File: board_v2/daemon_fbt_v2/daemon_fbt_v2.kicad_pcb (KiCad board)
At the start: 2 copper layers, 58 parts, among them IC1 NPM1100-QDAA-R7, IC2 nRF52840-QFAA-F-R7, IC3 MX25R6435FZAIL0-TR, J1 P70-5100045, J2 P70-5100045, J3 150mAh, Q1 FDV303N, U1 BMM350, U2 BHI360, Y1 ECS-320-8-37B2-CTN-TR

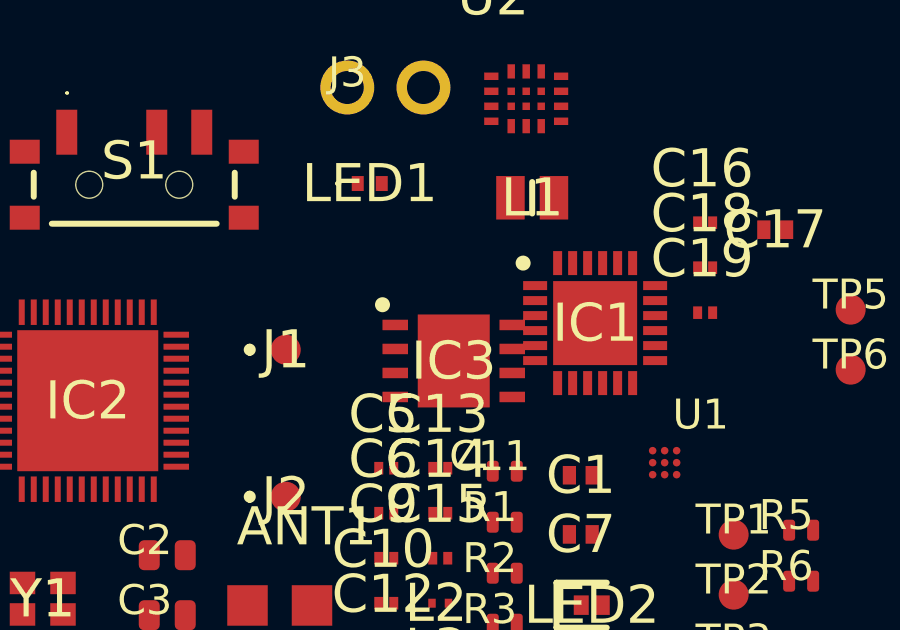
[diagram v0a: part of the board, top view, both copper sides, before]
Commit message: update flash memory from 64Mbit to 2Mbit and create footprint
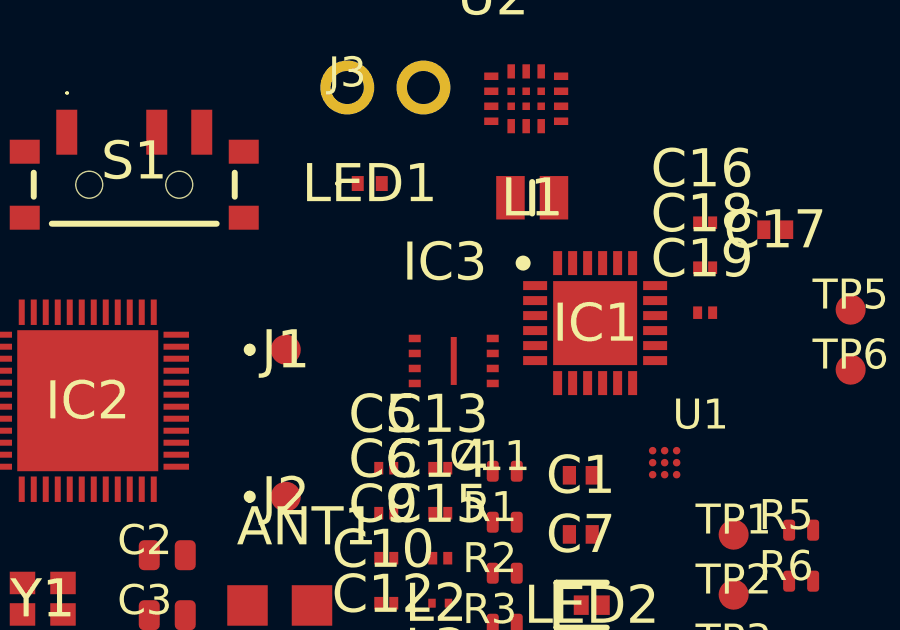
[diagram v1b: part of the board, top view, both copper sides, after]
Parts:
- IC3: value MX25R6435FZAIL0-TR -> MX25U2035FZUI-TR; footprint the_backrooms:SON80P400X400X60-9N -> the_backrooms:SON50P200X300X60-9N
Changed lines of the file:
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@@
     )
   )
-  (footprint "the_backrooms:SON80P400X400X60-9N" (layer "F.Cu")
+  (footprint "the_backrooms:SON50P200X300X60-9N" (layer "F.Cu")
     (at 39.57 33.01)
-    (descr "8-LAND USON (4x4mm)")
+    (descr "8-LAND USON (2x3mm)")
     (tags "Integrated Circuit")
     (property "Arrow Part Number" "")
     (property "Arrow Price/Stock" "")
+    (property "Description" "")
     (property "Height" "0.6")
     (property "Manufacturer_Name" "Macronix")
-    (property "Manufacturer_Part_Number" "MX25R6435FZAIL0-TR")
-    (property "Mfr. No." "MX25R6435FZAIL0-TR")
-    (property "Mouser Part Number" "95-25R6435FZAIL0TR")
-    (property "Mouser Price/Stock" "https://www.mouser.co.uk/ProductDetail/Macronix/MX25R6435FZAIL0-TR?qs=mELouGlnn3cK%252BXKdc9RzBg%3D%3D")
+    (property "Manufacturer_Part_Number" "MX25U2035FZUI-TR")
+    (property "Mfr. No." "MX25U2035FZUI-TR")
+    (property "Mouser Part Number" "MX25U2035FZUI-TR")
+    (property "Mouser Price/Stock" "")
+    (property "Package/Case" "")
     (property "Sheetfile" "daemon_fbt_v2.kicad_sch")
     (property "Sheetname" "")
     (property "ki_description" "NOR Flash Serial NOR 1.65V-3.6V 64Mbit x4 I/O USON-8 4x4mm")
     (attr smd)
-    (fp_text reference "IC3" (at 0 0) (layer "F.SilkS")
+    (fp_text reference "IC3" (at -0.3 -3.3) (layer "F.SilkS")
         (effects (font (size 1.27 1.27) (thickness 0.254)))
     )
-    (fp_text value "MX25R6435FZAIL0-TR" (at 0 0) (layer "F.SilkS") hide
+    (fp_text value "MX25U2035FZUI-TR" (at 0.2 3.3) (layer "F.SilkS") hide
         (effects (font (size 1.27 1.27) (thickness 0.254)))
     )
-    (fp_text user "${REFERENCE}" (at 0 0) (layer "F.Fab")
+    (fp_text user "${REFERENCE}" (at -0.1 3.4) (layer "F.Fab")
         (effects (font (size 1.27 1.27) (thickness 0.254)))
     )
-    (fp_circle (center -2.375 -1.875) (end -2.375 -1.75)
-      (stroke (width 0.25) (type solid)) (fill none) (layer "F.SilkS"))
-    (fp_line (start -2.625 -2.3) (end 2.625 -2.3)
-      (stroke (width 0.05) (type solid)) (layer "F.CrtYd"))
-    (fp_line (start -2.625 2.3) (end -2.625 -2.3)
-      (stroke (width 0.05) (type solid)) (layer "F.CrtYd"))
-    (fp_line (start 2.625 -2.3) (end 2.625 2.3)
-      (stroke (width 0.05) (type solid)) (layer "F.CrtYd"))
-    (fp_line (start 2.625 2.3) (end -2.625 2.3)
-      (stroke (width 0.05) (type solid)) (layer "F.CrtYd"))
-    (fp_line (start -2 -2) (end 2 -2)
-      (stroke (width 0.1) (type solid)) (layer "F.Fab"))
-    (fp_line (start -2 -1) (end -1 -2)
-      (stroke (width 0.1) (type solid)) (layer "F.Fab"))
-    (fp_line (start -2 2) (end -2 -2)
-      (stroke (width 0.1) (type solid)) (layer "F.Fab"))
-    (fp_line (start 2 -2) (end 2 2)
-      (stroke (width 0.1) (type solid)) (layer "F.Fab"))
-    (fp_line (start 2 2) (end -2 2)
-      (stroke (width 0.1) (type solid)) (layer "F.Fab"))
-    (pad "1" smd rect (at -1.95 -1.2 90) (size 0.35 0.85) (layers "F.Cu" "F.Paste" "F.Mask")
+    (fp_rect (start -1.5 -1) (end 1.5 1)
+      (stroke (width 0.1) (type default)) (fill none) (layer "Margin"))
+    (pad "1" smd rect (at -1.3 -0.75 90) (size 0.25 0.4) (layers "F.Cu" "F.Paste" "F.Mask")
       (net 48 "/QSPI_~{CS}") (pinfunction "CS#") (pintype "passive"))
-    (pad "2" smd rect (at -1.95 -0.4 90) (size 0.35 0.85) (layers "F.Cu" "F.Paste" "F.Mask")
+    (pad "2" smd rect (at -1.3 -0.25 90) (size 0.25 0.4) (layers "F.Cu" "F.Paste" "F.Mask")
       (net 51 "/QSPI_1") (pinfunction "SO/SIO1") (pintype "passive"))
-    (pad "3" smd rect (at -1.95 0.4 90) (size 0.35 0.85) (layers "F.Cu" "F.Paste" "F.Mask")
+    (pad "3" smd rect (at -1.3 0.25 90) (size 0.25 0.4) (layers "F.Cu" "F.Paste" "F.Mask")
       (net 52 "/QSPI_2") (pinfunction "WP#/SIO2") (pintype "passive"))
-    (pad "4" smd rect (at -1.95 1.2 90) (size 0.35 0.85) (layers "F.Cu" "F.Paste" "F.Mask")
+    (pad "4" smd rect (at -1.3 0.75 90) (size 0.25 0.4) (layers "F.Cu" "F.Paste" "F.Mask")
       (net 5 "GND") (pinfunction "GND") (pintype "passive"))
-    (pad "5" smd rect (at 1.95 1.2 90) (size 0.35 0.85) (layers "F.Cu" "F.Paste" "F.Mask")
+    (pad "5" smd rect (at 1.3 0.75 90) (size 0.25 0.4) (layers "F.Cu" "F.Paste" "F.Mask")
       (net 50 "/QSPI_0") (pinfunction "SI/SIO0") (pintype "passive"))
-    (pad "6" smd rect (at 1.95 0.4 90) (size 0.35 0.85) (layers "F.Cu" "F.Paste" "F.Mask")
+    (pad "6" smd rect (at 1.3 0.25 90) (size 0.25 0.4) (layers "F.Cu" "F.Paste" "F.Mask")
       (net 49 "/QSPI_CLK") (pinfunction "SCLK") (pintype "passive"))
-    (pad "7" smd rect (at 1.95 -0.4 90) (size 0.35 0.85) (layers "F.Cu" "F.Paste" "F.Mask")
+    (pad "7" smd rect (at 1.3 -0.25 90) (size 0.25 0.4) (layers "F.Cu" "F.Paste" "F.Mask")
       (net 53 "/QSPI_3") (pinfunction "RESET#/SIO3__OR_HOLD#/SIO3") (pintype "passive"))
-    (pad "8" smd rect (at 1.95 -1.2 90) (size 0.35 0.85) (layers "F.Cu" "F.Paste" "F.Mask")
+    (pad "8" smd rect (at 1.3 -0.75 90) (size 0.25 0.4) (layers "F.Cu" "F.Paste" "F.Mask")
       (net 7 "+1V8") (pinfunction "VCC") (pintype "passive"))
-    (pad "9" smd rect (at 0 0) (size 2.4 3.1) (layers "F.Cu" "F.Paste" "F.Mask")
+    (pad "9" smd rect (at 0 0) (size 0.2 1.6) (layers "F.Cu" "F.Paste" "F.Mask")
       (net 5 "GND") (pinfunction "EP") (pintype "passive"))
-    (model "/home/denji/Documents/kicad_lib/3d/MX25R6435FZAIL0-TR.stp"
-      (offset (xyz 0 0 0))
-      (scale (xyz 1 1 1))
-      (rotate (xyz 0 0 0))
-    )
   )
   (footprint "the_backrooms:FHR1105PTR" (layer "F.Cu")

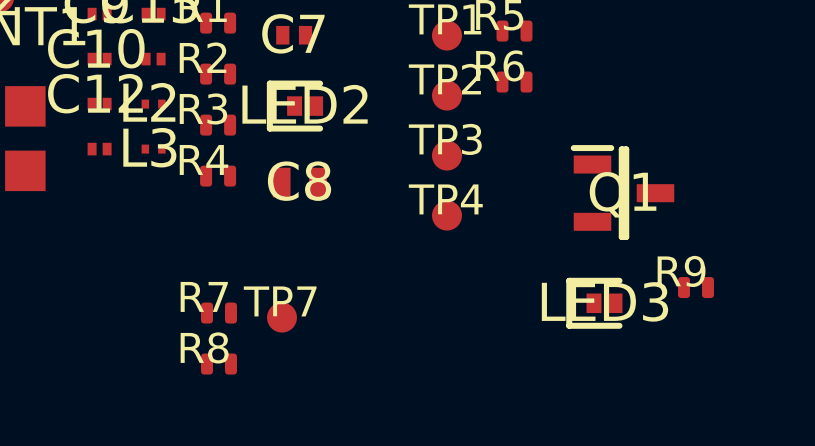
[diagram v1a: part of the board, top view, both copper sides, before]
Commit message: reduce price of some components
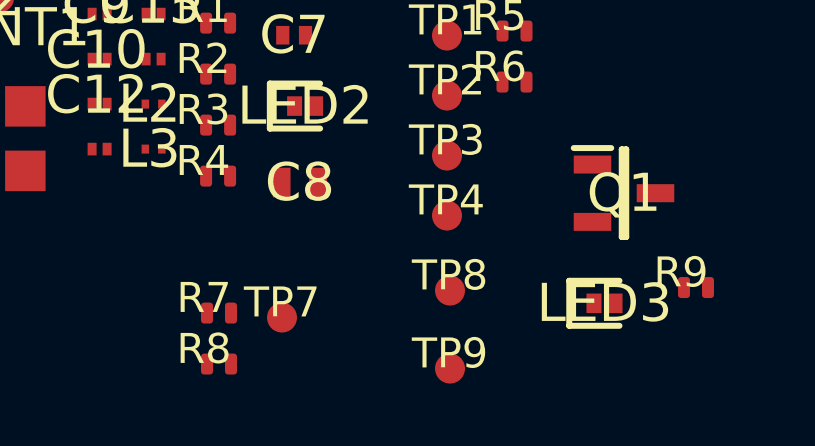
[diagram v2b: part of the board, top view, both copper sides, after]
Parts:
- added TP8: ~, the_backrooms:tp_1mm, F.Cu at (49.0, 47.3)
- added TP9: ~, the_backrooms:tp_1mm, F.Cu at (49.0, 49.9)
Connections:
- IC2 pad 15: unconnected-(IC2-P0.17-Pad15) -> /QSPI_~{CS}
- IC2 pad 16: /QSPI_~{CS} -> /~{RST}
- IC2 pad 19: unconnected-(IC2-P0.20-Pad19) -> /QSPI_0
- IC2 pad 20: /QSPI_0 -> /QSPI_1
- IC2 pad 21: /QSPI_1 -> /QSPI_2
- IC2 pad 22: /QSPI_2 -> /QSPI_3
- IC2 pad 24: /QSPI_3 -> /SWO

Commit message: finished redesign; lets hope jlcpcb doesn't kill me
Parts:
- removed S1: SSSS811101, the_backrooms:SSSS811101
- C8: footprint the_backrooms:CAPC1608X90N -> the_backrooms:CAPC1005X55N
- J1, J2, TP1, TP2, TP3, TP4, TP5, TP6, TP7, TP8, TP9: moved to B.Cu
- moved TP4 33.1 mm to (29.9, 17.7), turned to 180 degrees
- moved TP9 32.5 mm to (28.6, 24.6), turned to 90 degrees
- moved C23 32.4 mm to (27.5, 22.2), turned to 90 degrees
- moved R8 31.5 mm to (42.0, 18.2), turned to 180 degrees
- moved LED3 31.5 mm to (43.0, 18.2), turned to 180 degrees
- moved TP8 30.8 mm to (34.0, 20.4), turned to 90 degrees
- moved TP3 30.3 mm to (29.9, 19.2), turned to 180 degrees
- moved C24 30.3 mm to (27.7, 29.5), turned to 180 degrees
- moved R7 29.4 mm to (39.2, 18.7)
- moved TP7 27.8 mm to (37.2, 21.1), turned to -90 degrees
- moved C22 27.8 mm to (32.3, 21.6), turned to 90 degrees
- moved TP2 27.2 mm to (27.0, 24.6), turned to 180 degrees
- moved TP1 27.0 mm to (27.0, 23.0), turned to 180 degrees
- moved R9 26.9 mm to (42.4, 24.4), turned to 90 degrees
- moved C4 26.1 mm to (40.6, 20.0), turned to 180 degrees
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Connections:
- C8 pad 1: GND -> +1V8
- C8 pad 2: +1V8 -> GND
- J3 pad 1: /VBATTERY -> /VBAT
- R5 pad 2: /VBATTERY -> /VBAT
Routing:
- net GND: track 0.00 -> 51.1 mm, vias 0 -> 30
- net +1V8: track 0.00 -> 33.8 mm, vias 0 -> 11
- net /VBAT: track 0.00 -> 22.0 mm, vias 0 -> 2
- net /DEC_4_6: track 0.00 -> 12.9 mm, vias 0 -> 2
- net VBUS: track 0.00 -> 12.7 mm, vias 0 -> 2
- net /BAT_LOW: track 0.00 -> 10.7 mm, vias 0 -> 2
- net /VSYS: track 0.00 -> 10.2 mm, vias 0 -> 6
- net /SHPACT: track 0.00 -> 9.73 mm, vias 0 -> 2
- net /QSPI_~{CS}: track 0.00 -> 9.14 mm, vias 0 -> 2
- net /BHI360_INT: track 0.00 -> 8.47 mm, vias 0 -> 2
- net /QSPI_1: track 0.00 -> 7.40 mm, vias 0 -> 2
- net /CHG_LED: track 0.00 -> 7.07 mm, vias 0 -> 2
- net /ERR_LED: track 0.00 -> 6.59 mm, vias 0 -> 2
- net /BMM350_INT: track 0.00 -> 6.50 mm, vias 0 -> 2
- net Net-(ANT1-FEED): track 0.00 -> 5.93 mm
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- added copper zone on In2.Cu, net +1V8
- added copper zone on In2.Cu, net /VSYS
- added copper zone on B.Cu, net GND
- added copper zone on In1.Cu, net GND
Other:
- board outline added: 20 x 14 mm
- copper layers 2 -> 4

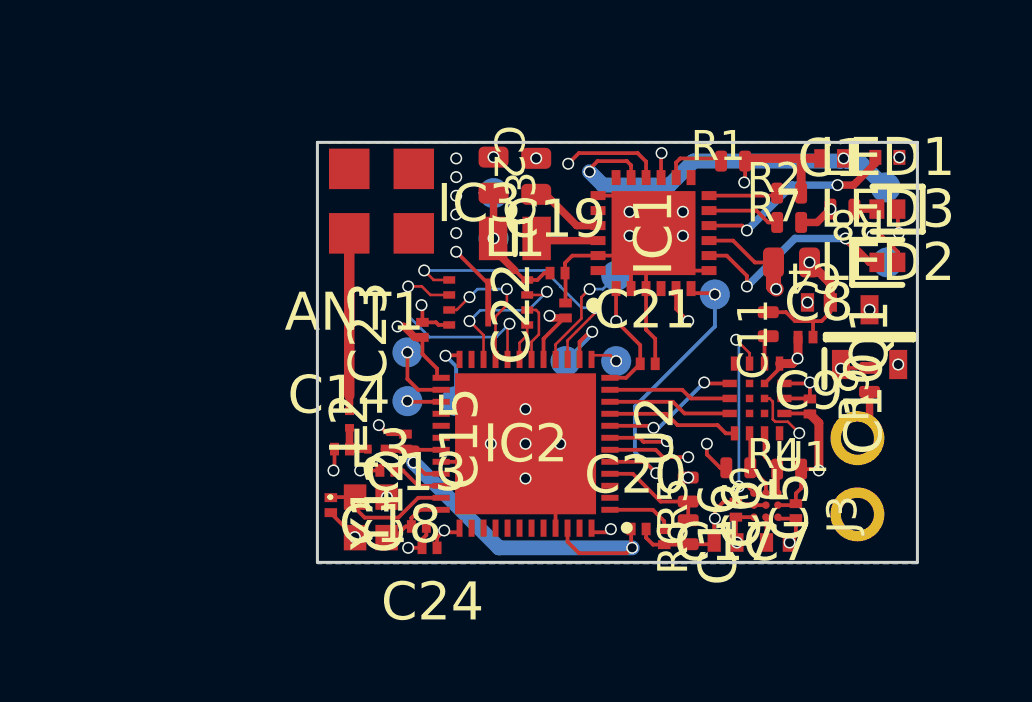
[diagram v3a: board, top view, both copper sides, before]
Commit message: redesign again, because there is no reason to make it very small; bc the size is battery limited
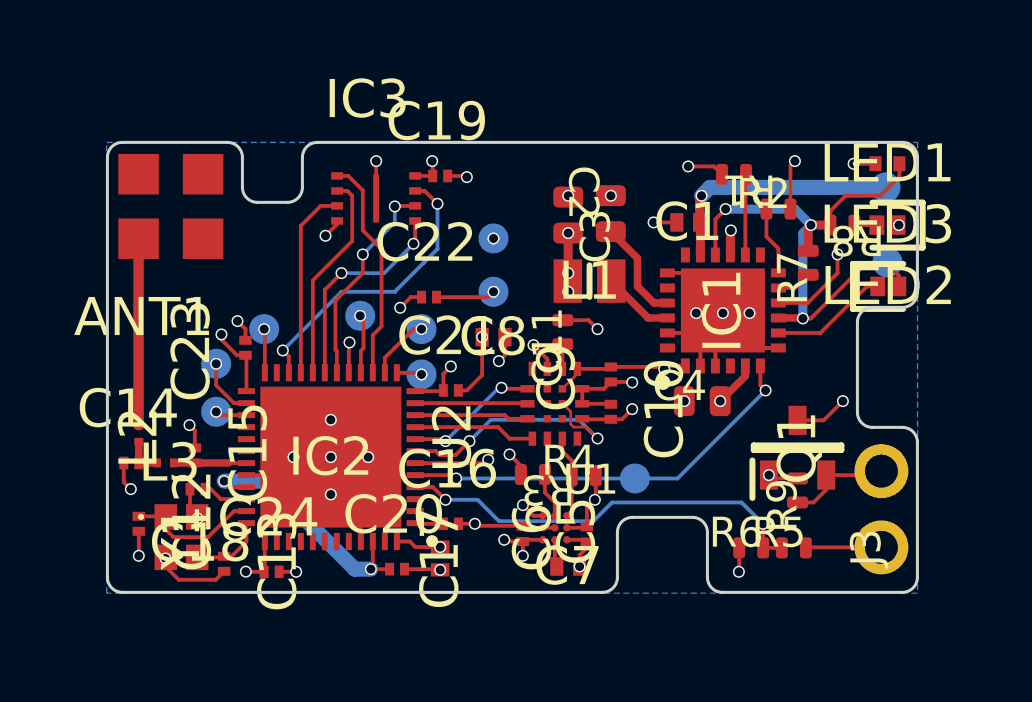
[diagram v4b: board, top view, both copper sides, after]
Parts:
- moved C8 10.9 mm to (29.9, 22.5), turned to 180 degrees
- moved C17 9.53 mm to (28.1, 29.9), turned to -90 degrees
- moved TP8 8.64 mm to (25.4, 21.8)
- moved C20 8.16 mm to (26.7, 30.2)
- moved C5 7.15 mm to (30.8, 29.1)
- moved C16 7.13 mm to (28.4, 28.7), turned to 0 degrees
- moved U1 7.07 mm to (31.5, 28.4)
- moved C14 7.04 mm to (17.8, 26.7)
- moved C15 7.04 mm to (19.9, 26.4)
- moved L2 7.04 mm to (18.0, 25.7)
- moved L3 7.04 mm to (18.9, 26.7)
- moved C7 7.04 mm to (32.4, 30.1)
- moved ANT1 7.03 mm to (19.1, 18.1)
- moved C6 7.01 mm to (33.0, 29.1)
- moved C11 6.85 mm to (32.2, 22.8)
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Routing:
- net /VSYS: track 10.2 -> 23.9 mm, vias 6 -> 4
- net /BAT_LVL: track 3.48 -> 14.0 mm, vias 0 -> 2
- net +1V8: track 33.8 -> 24.4 mm, vias 11 -> 18
- net /QSPI_0: track 1.12 -> 7.14 mm, vias 0 -> 2
- net /QSPI_CLK: track 1.95 -> 7.07 mm, vias 0 -> 2
- net /QSPI_3: track 5.02 -> 9.82 mm
- net /BAT_LOW: track 10.7 -> 15.5 mm
- net /VBAT: track 22.0 -> 17.2 mm, vias 2 -> 1
- net Net-(LED3-K): track 3.77 -> 8.42 mm
- net VBUS: track 12.7 -> 8.26 mm, vias 2 -> 1
- net /DEC_4_6: track 12.9 -> 8.50 mm
- net /SHPACT: track 9.73 -> 13.8 mm
- net /CHG_LED: track 7.07 -> 3.95 mm, vias 2 -> 0
- net GND: track 51.1 -> 49.2 mm, vias 30 -> 32
- net /QSPI_2: track 4.57 -> 6.38 mm, vias 2 -> 0
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- removed copper zone on In2.Cu, net /VSYS
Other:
- board size 20 x 14 mm -> 27 x 15 mm
